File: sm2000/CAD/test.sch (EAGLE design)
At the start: 31 parts, among them Q1 BRF92, Q2 BFQ19, Q3 BFQ19, X1 BU-SMA-G, X2 BU-SMA-G

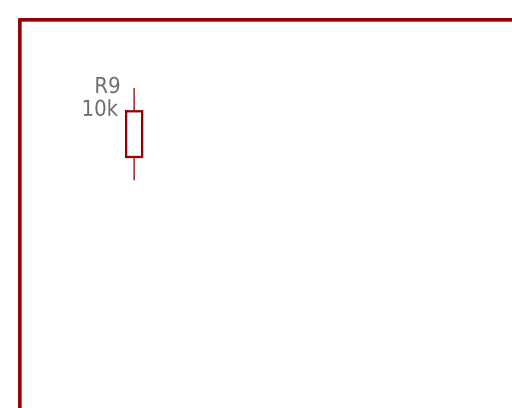
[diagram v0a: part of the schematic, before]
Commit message: test - removed resistor from schematic
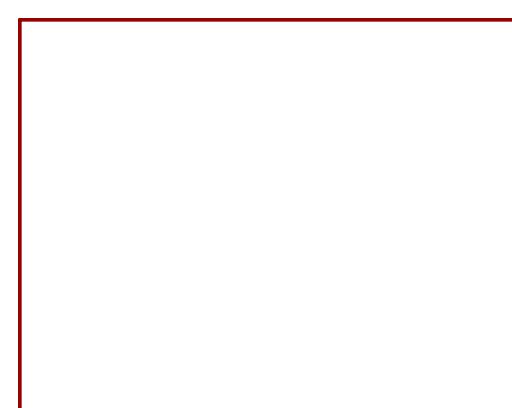
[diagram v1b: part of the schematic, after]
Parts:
- removed R9: 10k, AA-ipc-7351-resistor:RESISTOR_0805
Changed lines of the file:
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@@
 <part name="C10" library="_RoweTel" deviceset="TRIMCAP_VAR_2222_V" device=""/>
 <part name="U$1" library="A-FRAMES" deviceset="ROWE-ASIZE" device=""/>
-<part name="R9" library="AA-ipc-7351-resistor" deviceset="RESISTOR_" device="0805" value="10k"/>
 </parts>
 <sheets>
@@
 <instance part="U$1" gate="G$2" x="147.32" y="0"/>
 <instance part="U$1" gate="G$3" x="175.26" y="185.42"/>
-<instance part="R9" gate="G$1" x="12.7" y="172.72" smashed="yes" rot="R90">
-<attribute name="NAME" x="11.2014" y="179.07" size="1.778" layer="95" rot="R180"/>
-<attribute name="VALUE" x="10.922" y="176.53" size="1.778" layer="96" rot="R180"/>
-</instance>
 </instances>
 <busses>

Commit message: 
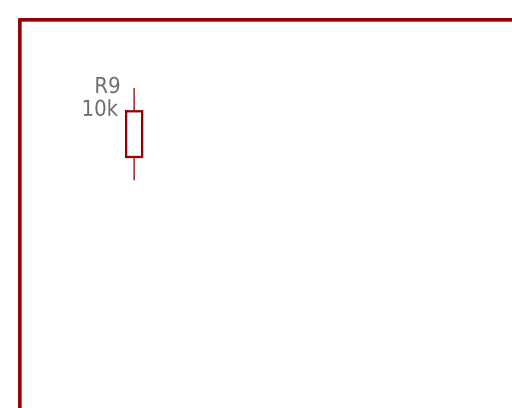
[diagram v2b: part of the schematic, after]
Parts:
- added R9: 10k, AA-ipc-7351-resistor:RESISTOR_0805
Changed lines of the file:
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@@
 <part name="C10" library="_RoweTel" deviceset="TRIMCAP_VAR_2222_V" device=""/>
 <part name="U$1" library="A-FRAMES" deviceset="ROWE-ASIZE" device=""/>
+<part name="R9" library="AA-ipc-7351-resistor" deviceset="RESISTOR_" device="0805" value="10k"/>
 </parts>
 <sheets>
@@
 <instance part="U$1" gate="G$2" x="147.32" y="0"/>
 <instance part="U$1" gate="G$3" x="175.26" y="185.42"/>
+<instance part="R9" gate="G$1" x="12.7" y="172.72" smashed="yes" rot="R90">
+<attribute name="NAME" x="11.2014" y="179.07" size="1.778" layer="95" rot="R180"/>
+<attribute name="VALUE" x="10.922" y="176.53" size="1.778" layer="96" rot="R180"/>
+</instance>
 </instances>
 <busses>
